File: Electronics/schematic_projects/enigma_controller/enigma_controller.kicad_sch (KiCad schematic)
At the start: 64 parts, among them IC1 TPD8S300ARUKR, IC10 MCP23017-E_SO, IC2 ESD321DYAR, IC3 ESD321DYAR, IC9 MCP23017-E_SO, J1 Conn_02x05_Odd_Even, J11 Conn_02x05_Odd_Even, J12 Conn_01x02, J15 Conn_01x02, J16 Conn_01x02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

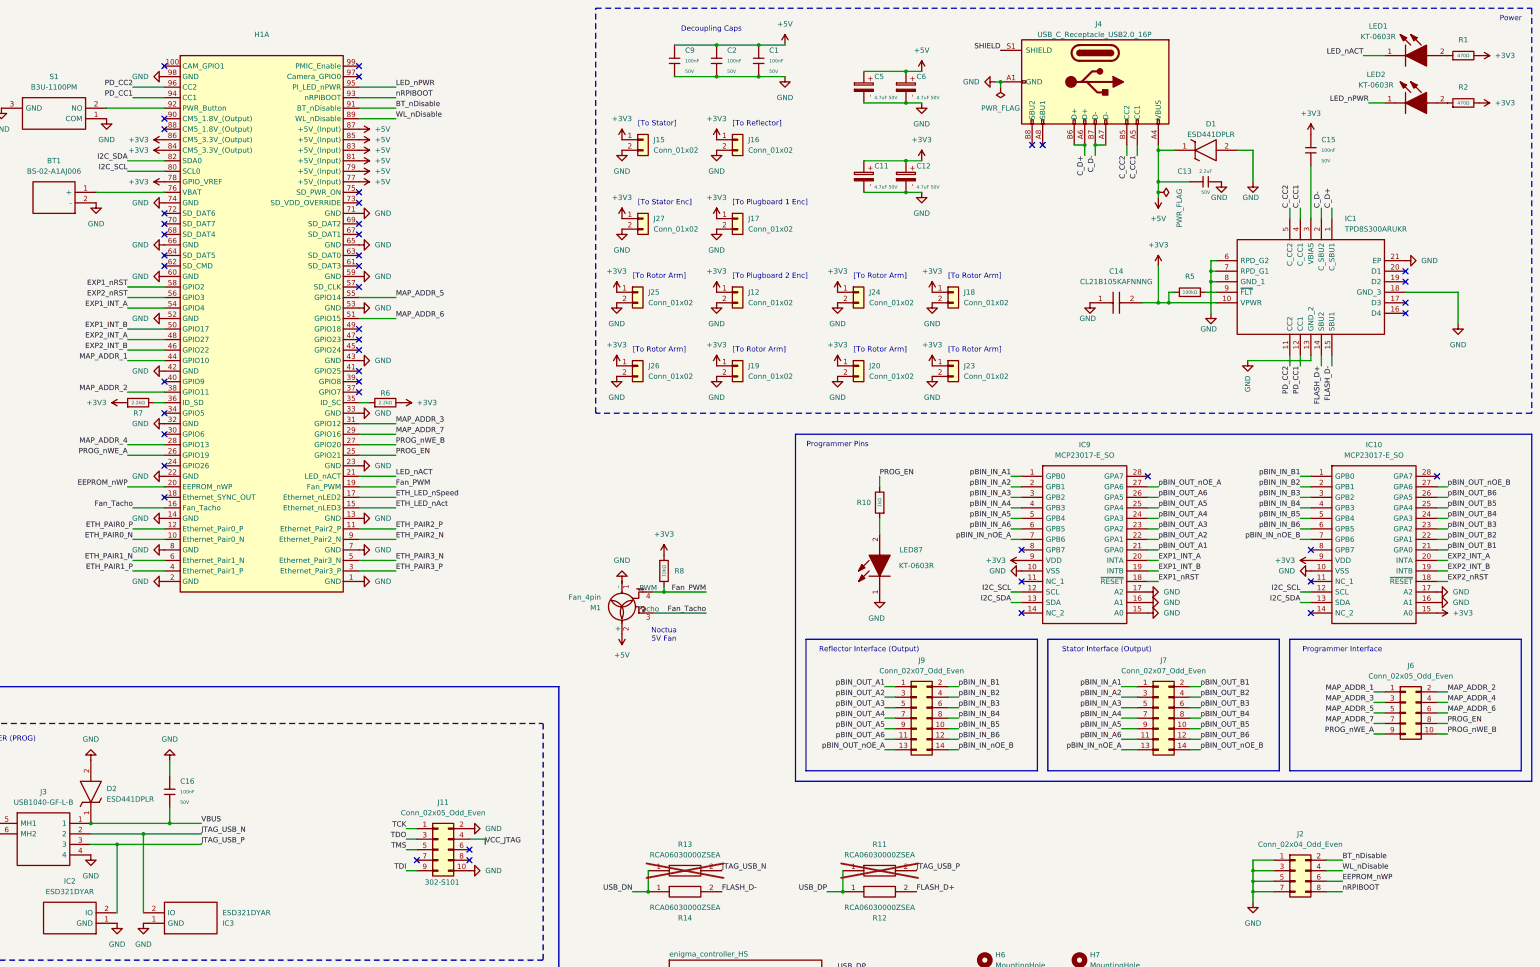
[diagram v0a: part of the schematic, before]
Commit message: Updated for impedance calculated trace widths.
Also added slow signals and traces for ESD protection components.
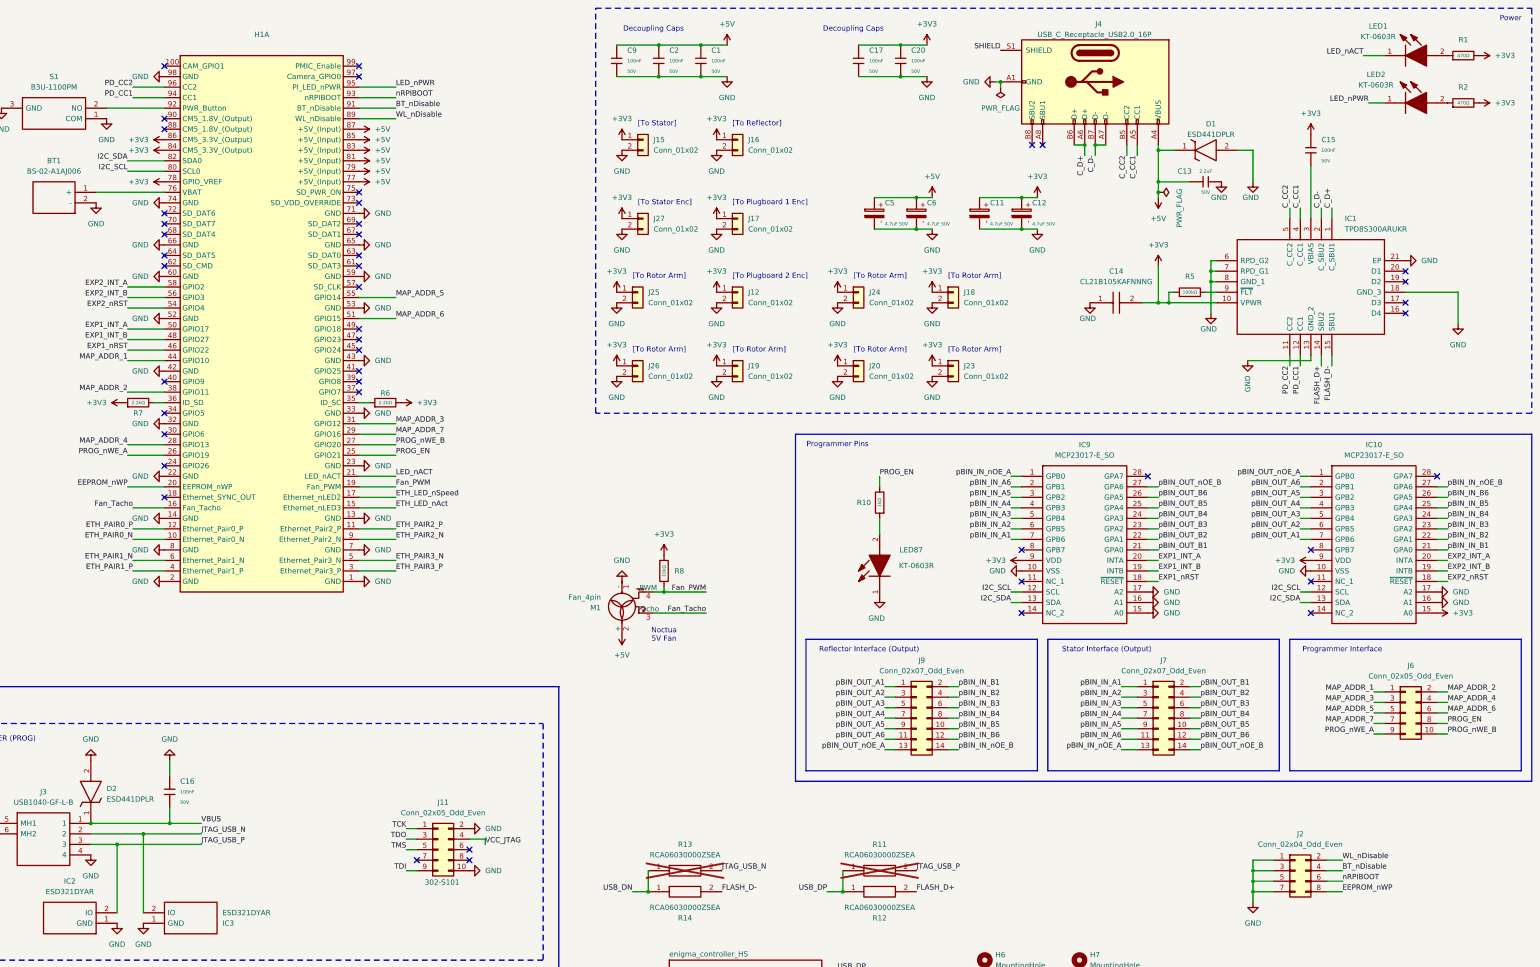
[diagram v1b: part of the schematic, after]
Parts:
- added C17, C20: 100nF, PCM_JLCPCB:C_0402, symbol PCM_JLCPCB-Capacitors:0402,100nF,(2)
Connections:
- net +3V3: now also C17.1, C20.1
- net BT_nDisable: now also J2.4 (Pin_4); no longer J2.2 (Pin_2)
- net EEPROM_nWP: now also J2.8 (Pin_8); no longer J2.6 (Pin_6)
- net EXP1_INT_A: now also H1.50 (GPIO17); no longer H1.54 (GPIO4)
- net EXP1_INT_B: now also H1.48 (GPIO27); no longer H1.50 (GPIO17)
- net EXP1_nRST: now also H1.46 (GPIO22); no longer H1.58 (GPIO2)
- net EXP2_INT_A: now also H1.58 (GPIO2); no longer H1.48 (GPIO27)
- net EXP2_INT_B: now also H1.56 (GPIO3); no longer H1.46 (GPIO22)
- net EXP2_nRST: now also H1.54 (GPIO4); no longer H1.56 (GPIO3)
- net GND: now also C17.2, C20.2
- net WL_nDisable: now also J2.2 (Pin_2); no longer J2.4 (Pin_4)
- net nRPIBOOT: now also J2.6 (Pin_6); no longer J2.8 (Pin_8)
- net pBIN_IN_A1: now also IC9.7 (GPB6); no longer IC9.1 (GPB0)
- net pBIN_IN_A2: now also IC9.6 (GPB5); no longer IC9.2 (GPB1)
- net pBIN_IN_A3: now also IC9.5 (GPB4); no longer IC9.3 (GPB2)
- net pBIN_IN_A5: now also IC9.3 (GPB2); no longer IC9.5 (GPB4)
- net pBIN_IN_A6: now also IC9.2 (GPB1); no longer IC9.6 (GPB5)
- net pBIN_IN_B1: now also IC10.21 (GPA0); no longer IC10.1 (GPB0)
- net pBIN_IN_B2: now also IC10.22 (GPA1); no longer IC10.2 (GPB1)
- net pBIN_IN_B3: now also IC10.23 (GPA2); no longer IC10.3 (GPB2)
- net pBIN_IN_B4: now also IC10.24 (GPA3); no longer IC10.4 (GPB3)
- net pBIN_IN_B5: now also IC10.25 (GPA4); no longer IC10.5 (GPB4)
- net pBIN_IN_B6: now also IC10.26 (GPA5); no longer IC10.6 (GPB5)
- net pBIN_IN_nOE_A: now also IC9.1 (GPB0); no longer IC9.7 (GPB6)
- net pBIN_IN_nOE_B: now also IC10.27 (GPA6); no longer IC10.7 (GPB6)
- net pBIN_OUT_A1: now also IC10.7 (GPB6); no longer IC9.21 (GPA0)
- net pBIN_OUT_A2: now also IC10.6 (GPB5); no longer IC9.22 (GPA1)
- net pBIN_OUT_A3: now also IC10.5 (GPB4); no longer IC9.23 (GPA2)
- net pBIN_OUT_A4: now also IC10.4 (GPB3); no longer IC9.24 (GPA3)
- net pBIN_OUT_A5: now also IC10.3 (GPB2); no longer IC9.25 (GPA4)
- net pBIN_OUT_A6: now also IC10.2 (GPB1); no longer IC9.26 (GPA5)
- net pBIN_OUT_B1: now also IC9.21 (GPA0); no longer IC10.21 (GPA0)
- net pBIN_OUT_B2: now also IC9.22 (GPA1); no longer IC10.22 (GPA1)
- net pBIN_OUT_B3: now also IC9.23 (GPA2); no longer IC10.23 (GPA2)
- net pBIN_OUT_B4: now also IC9.24 (GPA3); no longer IC10.24 (GPA3)
- net pBIN_OUT_B5: now also IC9.25 (GPA4); no longer IC10.25 (GPA4)
- net pBIN_OUT_B6: now also IC9.26 (GPA5); no longer IC10.26 (GPA5)
- net pBIN_OUT_nOE_A: now also IC10.1 (GPB0); no longer IC9.27 (GPA6)
- net pBIN_OUT_nOE_B: now also IC9.27 (GPA6); no longer IC10.27 (GPA6)
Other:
- moved on the sheet: C1, C11, C12, C2, C5, C6, C9

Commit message: Updated for new battery holder.
Also updated 3d models for components and fixed skew and trace lengths for main high-speed lines.
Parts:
- removed BT1: BS-02-A1AJ006, Enigma_Components:BS02A1AJ006, symbol Enigma_Components:BS-02-A1AJ006
- removed R11, R12, R13, R14: RCA06030000ZSEA, Enigma_Components:RESC1608X50N, symbol Enigma_Components:RCA06030000ZSEA
- added BT1: CR2032-BS-6-1, Enigma_Components:CR2032BS61, symbol Enigma_Components:CR2032-BS-6-1
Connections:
- net GND: now also BT1.2 (-)
- net at H1.76 (VBAT): now also BT1.1 (+)
- removed net C_D+: IC1.1 (C_SBU1), J4.A6 (D+), J4.B6 (D+)
- removed net C_D-: IC1.2 (C_SBU2), J4.A7 (D-), J4.B7 (D-)
- net FLASH_D+: no longer names the net of IC1.14 (SBU2)
- net FLASH_D-: no longer names the net of IC1.15 (SBU1)
- no-connect marks 54 -> 62

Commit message: Updated with board-2-board connectors.
Also re-organised components to reduce PCB size.
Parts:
- removed J12, J15, J16, J17, J18, J19, J20, J23, J24, J25, J26, J27: Conn_01x02, Connector_PinHeader_2.54mm:PinHeader_1x02_P2.54mm_Vertical, symbol Connector_Generic:Conn_01x02
- removed J2: Conn_02x04_Odd_Even, Connector_PinHeader_2.54mm:PinHeader_2x04_P2.54mm_Vertical, symbol Connector_Generic:Conn_02x04_Odd_Even
- removed J6: Conn_02x05_Odd_Even, Connector_IDC:IDC-Header_2x05_P2.54mm_Vertical, symbol Connector_Generic:Conn_02x05_Odd_Even
- removed J7, J9: Conn_02x07_Odd_Even, Connector_IDC:IDC-Header_2x07_P2.54mm_Vertical, symbol Connector_Generic:Conn_02x07_Odd_Even
- added H8: MountingHole, MountingHole:MountingHole_4.3mm_M4, symbol Mechanical:MountingHole
- added J2: Conn_02x02_Odd_Even, Connector_PinHeader_2.54mm:PinHeader_2x02_P2.54mm_Vertical, symbol Connector_Generic:Conn_02x02_Odd_Even
- added J6: ESW-120-33-G-D, ESW-120-XX-Y-D, symbol Enigma_Components:ESW-120-33-G-D
- J1, J21, J22: footprint Connector_IDC:IDC-Header_2x05_P2.54mm_Vertical -> Connector_IDC:IDC-Header_2x05_P2.54mm_Horizontal
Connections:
- net +3V3: now also J6.25
- net BT_nDisable: now also J2.4 (Pin_4)
- net GND: now also J1.4 (Pin_4), J1.6 (Pin_6), J1.8 (Pin_8), J21.4 (Pin_4), J21.6 (Pin_6), J21.8 (Pin_8), J22.4 (Pin_4), J22.6 (Pin_6), J22.8 (Pin_8), J2.1 (Pin_1), J2.3 (Pin_3), J6.26
- net MAP_ADDR_1: now also J6.9
- net MAP_ADDR_2: now also J6.10
- net MAP_ADDR_3: now also J6.7
- net MAP_ADDR_4: now also J6.8
- net MAP_ADDR_5: now also J6.5
- net MAP_ADDR_6: now also J6.6
- net MAP_ADDR_7: now also J6.3
- net PROG_EN: now also J6.4
- net PROG_nWE_A: now also J6.1
- net PROG_nWE_B: now also J6.2
- net TCK: now also J1.3 (Pin_3), J21.3 (Pin_3), J22.3 (Pin_3); no longer J1.1 (Pin_1), J21.1 (Pin_1), J22.1 (Pin_1)
- net TDO: now also J1.5 (Pin_5); no longer J1.3 (Pin_3)
- net TDX1: now also J22.5 (Pin_5); no longer J22.3 (Pin_3)
- net TDX2: now also J21.5 (Pin_5); no longer J21.3 (Pin_3)
- net TMS: now also J1.7 (Pin_7), J21.7 (Pin_7), J22.7 (Pin_7); no longer J1.5 (Pin_5), J21.5 (Pin_5), J22.5 (Pin_5)
- net VCC_JTAG: now also J1.1 (Pin_1), J21.1 (Pin_1), J22.1 (Pin_1); no longer J1.4 (Pin_4), J21.4 (Pin_4), J22.4 (Pin_4)
- net WL_nDisable: now also J2.2 (Pin_2)
- net pBIN_IN_A1: now also J6.39
- net pBIN_IN_A2: now also J6.37
- net pBIN_IN_A3: now also J6.35
- net pBIN_IN_A4: now also J6.33
- net pBIN_IN_A5: now also J6.31
- net pBIN_IN_A6: now also J6.29
- net pBIN_IN_B1: now also J6.24
- net pBIN_IN_B2: now also J6.22
- net pBIN_IN_B3: now also J6.20
- net pBIN_IN_B4: now also J6.18
- net pBIN_IN_B5: now also J6.16
- net pBIN_IN_B6: now also J6.14
- net pBIN_IN_nOE_A: now also J6.27
- net pBIN_IN_nOE_B: now also J6.12
- net pBIN_OUT_A1: now also J6.23
- net pBIN_OUT_A2: now also J6.21
- net pBIN_OUT_A3: now also J6.19
- net pBIN_OUT_A4: now also J6.17
- net pBIN_OUT_A5: now also J6.15
- net pBIN_OUT_A6: now also J6.13
- net pBIN_OUT_B1: now also J6.40
- net pBIN_OUT_B2: now also J6.38
- net pBIN_OUT_B3: now also J6.36
- net pBIN_OUT_B4: now also J6.34
- net pBIN_OUT_B5: now also J6.32
- net pBIN_OUT_B6: now also J6.30
- net pBIN_OUT_nOE_A: now also J6.11
- net pBIN_OUT_nOE_B: now also J6.28
- net EEPROM_nWP: no longer names the net of H1.20 (EEPROM_nWP)
- net nRPIBOOT: no longer names the net of H1.93 (nRPIBOOT)
- no-connect marks 62 -> 55
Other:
- note removed: "Programmer Interface"
- note removed: "Reflector Interface (Output)"
- note removed: "Stator Interface (Output)"
- note removed: "[To Plugboard 1 Enc]"
- note removed: "[To Plugboard 2 Enc]"
- note removed: "[To Reflector]"
- note removed: "[To Rotor Arm]"
- note removed: "[To Stator Enc]"
- note removed: "[To Stator]"
- moved on the sheet: C1, C11, C12, C13, C14, C15, C16, C17, C2, C20, C5, C6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

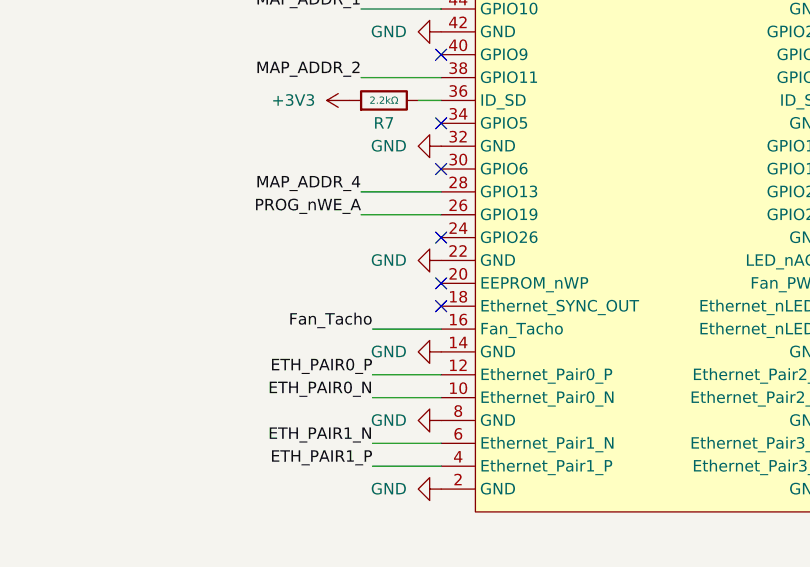
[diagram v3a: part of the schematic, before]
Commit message: Slight re-organisation of USB current limiter.
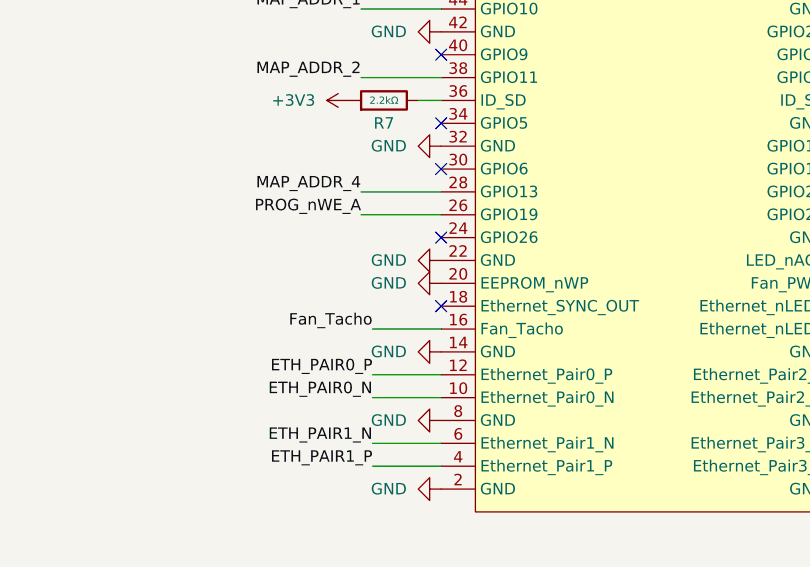
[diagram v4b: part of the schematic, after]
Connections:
- net GND: now also H1.20 (EEPROM_nWP)
- no-connect marks 55 -> 54
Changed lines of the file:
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@@
 	)
 	(no_connect
-		(at 73.66 133.35)
-	)
-	(no_connect
 		(at 73.66 67.31)
 	)
@@
 					(unit 1)
 				)
+			)
+		)
+	)
+	(symbol
+		(lib_id "power:GND")
+		(at 73.66 133.35 270)
+		(unit 1)
+		(exclude_from_sim no)
+		(in_bom yes)
+		(on_board yes)
+		(dnp no)
+		(fields_autoplaced yes)
+		(property "Reference" "#PWR069"
+			(at 67.31 133.35 0)
+			(effects
+				(font
+					(size 1.27 1.27)
+				)
+				(hide yes)
+			)
+		)
+		(property "Value" "GND"
+			(at 69.85 133.3499 90)
+			(effects
+				(font
+					(size 1.27 1.27)
+				)
+				(justify right)
+			)
+		)
+		(property "Footprint" ""
+			(at 73.66 133.35 0)
+			(effects
+				(font
+					(size 1.27 1.27)
+				)
+				(hide yes)
+			)
+		)
+		(property "Datasheet" ""
+			(at 73.66 133.35 0)
+			(effects
+				(font
+					(size 1.27 1.27)
+				)
+				(hide yes)
+			)
+		)
+		(property "Description" "Power symbol creates a global label with name \"GND\" , ground"
+			(at 73.66 133.35 0)
+			(effects
+				(font
+					(size 1.27 1.27)
+				)
+				(hide yes)
+			)
+		)
+		(pin "1"
+		)
+		(instances
+			(project "enigma_controller"
+				(path "/f6846724-845b-4e7d-9c42-5003d8826a6e"
+					(reference "#PWR069")
+					(unit 1)
+				)
